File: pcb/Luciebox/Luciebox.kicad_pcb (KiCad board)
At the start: 2 copper layers, 100 x 100 mm, 91 parts, among them J1 Screw_Terminal_01x07, J2 Screw_Terminal_01x07, J3 Screw_Terminal_01x07, J4 Screw_Terminal_01x07, J5 Screw_Terminal_01x07, P1 CONN_01X01, P2 CONN_01X01, P3 CONN_01X01, P4 CONN_01X01, P5 Digital, P6 Power, P7 Digital, P8 Analog, Q1 BC558, Q2 N-Channel_Mosfet, T1 terminal_13x1, T10 terminal_8x1, T11 terminal_3x1, T2 terminal_8x1, T3 terminal_8x1, T4 terminal_8x1, T5 terminal_8x1, T6 terminal_8x1, T7 terminal_8x1, T8 terminal_8x1, T9 terminal_8x1, U1 CA56-12SRWA, U2 ULN2003A, U3 ATmega328-PU, Y1 16MHz

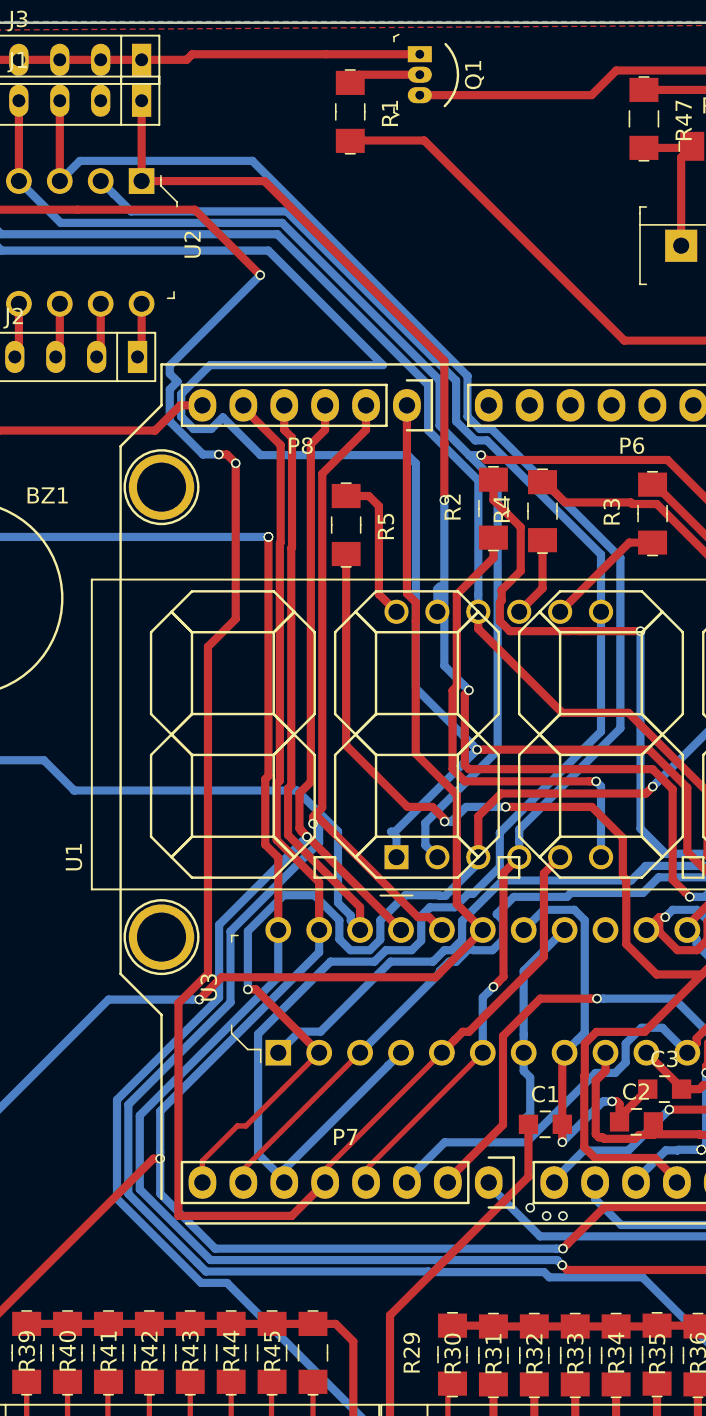
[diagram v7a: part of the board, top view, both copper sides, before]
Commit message: ah, now all traces are connected
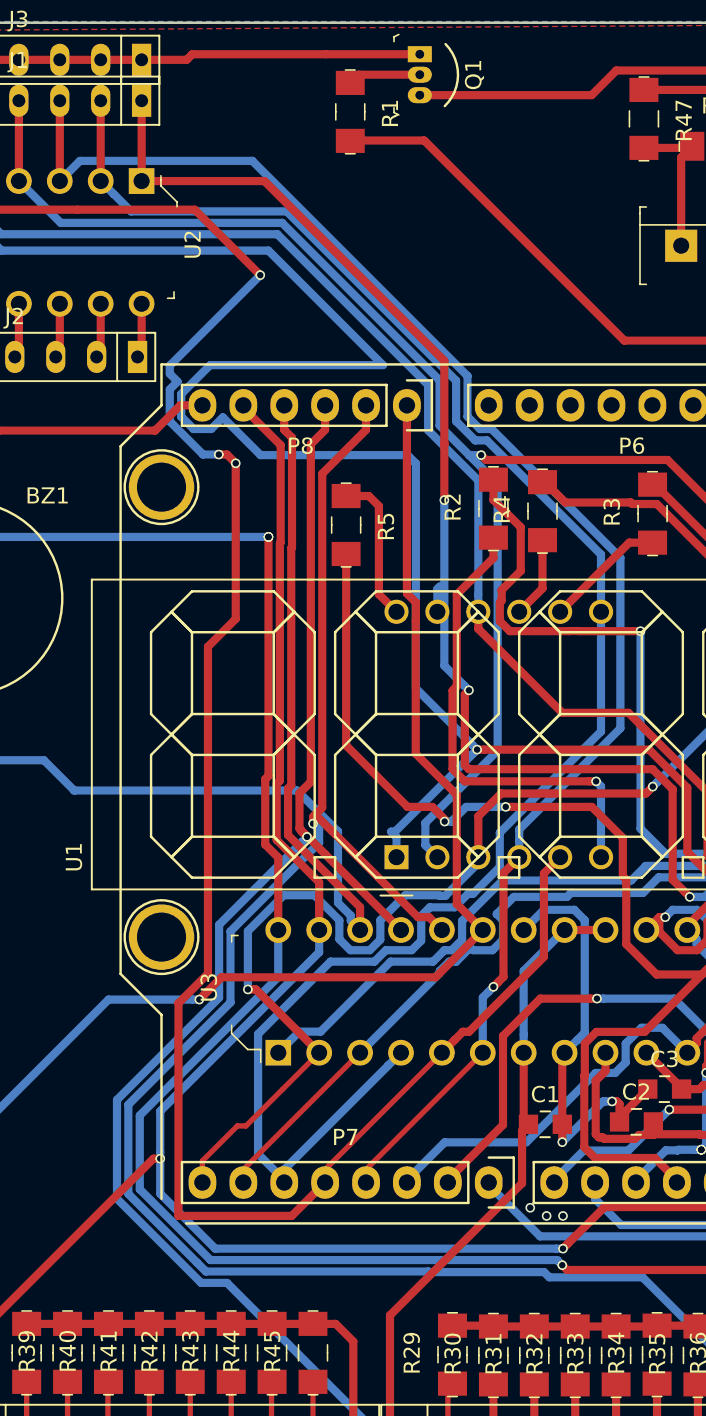
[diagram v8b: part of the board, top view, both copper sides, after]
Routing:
- net /2: track 105.3 -> 110.3 mm
- net VCC: track 291.2 -> 293.5 mm
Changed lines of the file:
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@@
   (segment (start 41.572798 57.807402) (end 40.864788 58.515412) (width 0.508) (layer B.Cu) (net 16))
   (segment (start 38.130386 58.515412) (end 33.635599 63.010199) (width 0.508) (layer B.Cu) (net 16))
+  (segment (start 23.863475 10.046) (end 23.863475 5.056977) (width 0.508) (layer F.Cu) (net 16))
   (segment (start 32.7188 71.4242) (end 32.7188 72.2334) (width 0.3302) (layer F.Cu) (net 17))
   (segment (start 39.9696 64.1734) (end 32.7188 71.4242) (width 0.3302) (layer F.Cu) (net 17))
@@
   (segment (start 86.02601 2.49599) (end 86.02601 3.71801) (width 0.508) (layer F.Cu) (net 43))
   (segment (start 19.225522 98.071003) (end 37.005522 98.071003) (width 0.3302) (layer F.Cu) (net 44))
-  (segment (start 50.1296 65.30477) (end 50.536 65.71117) (width 0.508) (layer B.Cu) (net 44))
-  (segment (start 50.1296 64.1734) (end 50.1296 65.30477) (width 0.508) (layer B.Cu) (net 44))
-  (segment (start 50.536 65.71117) (end 50.536 67.958) (width 0.508) (layer B.Cu) (net 44))
-  (segment (start 50.536 67.958) (end 50.282 68.212) (width 0.508) (layer B.Cu) (net 44))
-  (segment (start 50.282 68.212) (end 50.282 68.72) (width 0.508) (layer B.Cu) (net 44))
   (segment (start 52.6696 56.5534) (end 50.1296 59.0934) (width 0.508) (layer B.Cu) (net 44))
   (segment (start 50.1296 59.0934) (end 50.1296 63.04203) (width 0.508) (layer B.Cu) (net 44))
@@
   (segment (start 83.556 98.057) (end 84.191 98.057) (width 0.508) (layer F.Cu) (net 44))
   (segment (start 86.731 98.057) (end 89.271 98.057) (width 0.508) (layer F.Cu) (net 44))
-  (segment (start 50.4258 68.6184) (end 50.4258 71.8782) (width 0.508) (layer F.Cu) (net 44))
-  (segment (start 41.829557 97.49256) (end 42.408 98.071003) (width 0.508) (layer F.Cu) (net 44))
-  (segment (start 41.829557 80.474443) (end 41.829557 97.49256) (width 0.508) (layer F.Cu) (net 44))
   (segment (start 37.005522 98.071003) (end 42.408 98.071003) (width 0.508) (layer F.Cu) (net 44))
-  (segment (start 50.4258 71.8782) (end 41.829557 80.474443) (width 0.508) (layer F.Cu) (net 44))
   (segment (start 42.408 98.071003) (end 45.441997 98.071003) (width 0.508) (layer F.Cu) (net 44))
   (segment (start 90.414 48.664) (end 93.071 51.321) (width 0.508) (layer F.Cu) (net 44))
@@
   (segment (start 91.557 98.057) (end 89.271 98.057) (width 0.508) (layer F.Cu) (net 44))
   (segment (start 91.684 98.184) (end 91.557 98.057) (width 0.508) (layer F.Cu) (net 44))
+  (segment (start 52.6696 56.5534) (end 55.2096 56.5534) (width 0.508) (layer F.Cu) (net 44))
+  (segment (start 41.829557 97.49256) (end 42.408 98.071003) (width 0.508) (layer F.Cu) (net 44))
+  (segment (start 50.4258 68.6184) (end 50.028 69.0162) (width 0.508) (layer F.Cu) (net 44))
+  (segment (start 41.829557 80.474443) (end 41.829557 97.49256) (width 0.508) (layer F.Cu) (net 44))
+  (segment (start 50.028 72.276) (end 41.829557 80.474443) (width 0.508) (layer F.Cu) (net 44))
+  (segment (start 50.028 69.0162) (end 50.028 72.276) (width 0.508) (layer F.Cu) (net 44))
+  (segment (start 50.1296 68.3222) (end 50.4258 68.6184) (width 0.508) (layer F.Cu) (net 44))
+  (segment (start 50.1296 64.1734) (end 50.1296 68.3222) (width 0.508) (layer F.Cu) (net 44))
   (segment (start 72.138 65.926) (end 71.872 66.192) (width 0.508) (layer F.Cu) (net 45))
   (segment (start 71.872 66.192) (end 71.872 67.45) (width 0.508) (layer F.Cu) (net 45))
